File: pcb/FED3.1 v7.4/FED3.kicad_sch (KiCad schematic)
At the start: 29 parts, among them IC2 TB6612FNG, SW1 Sw, U2 MIC5504-3.3, U3 MCP73831T, X5 JST-XH-02

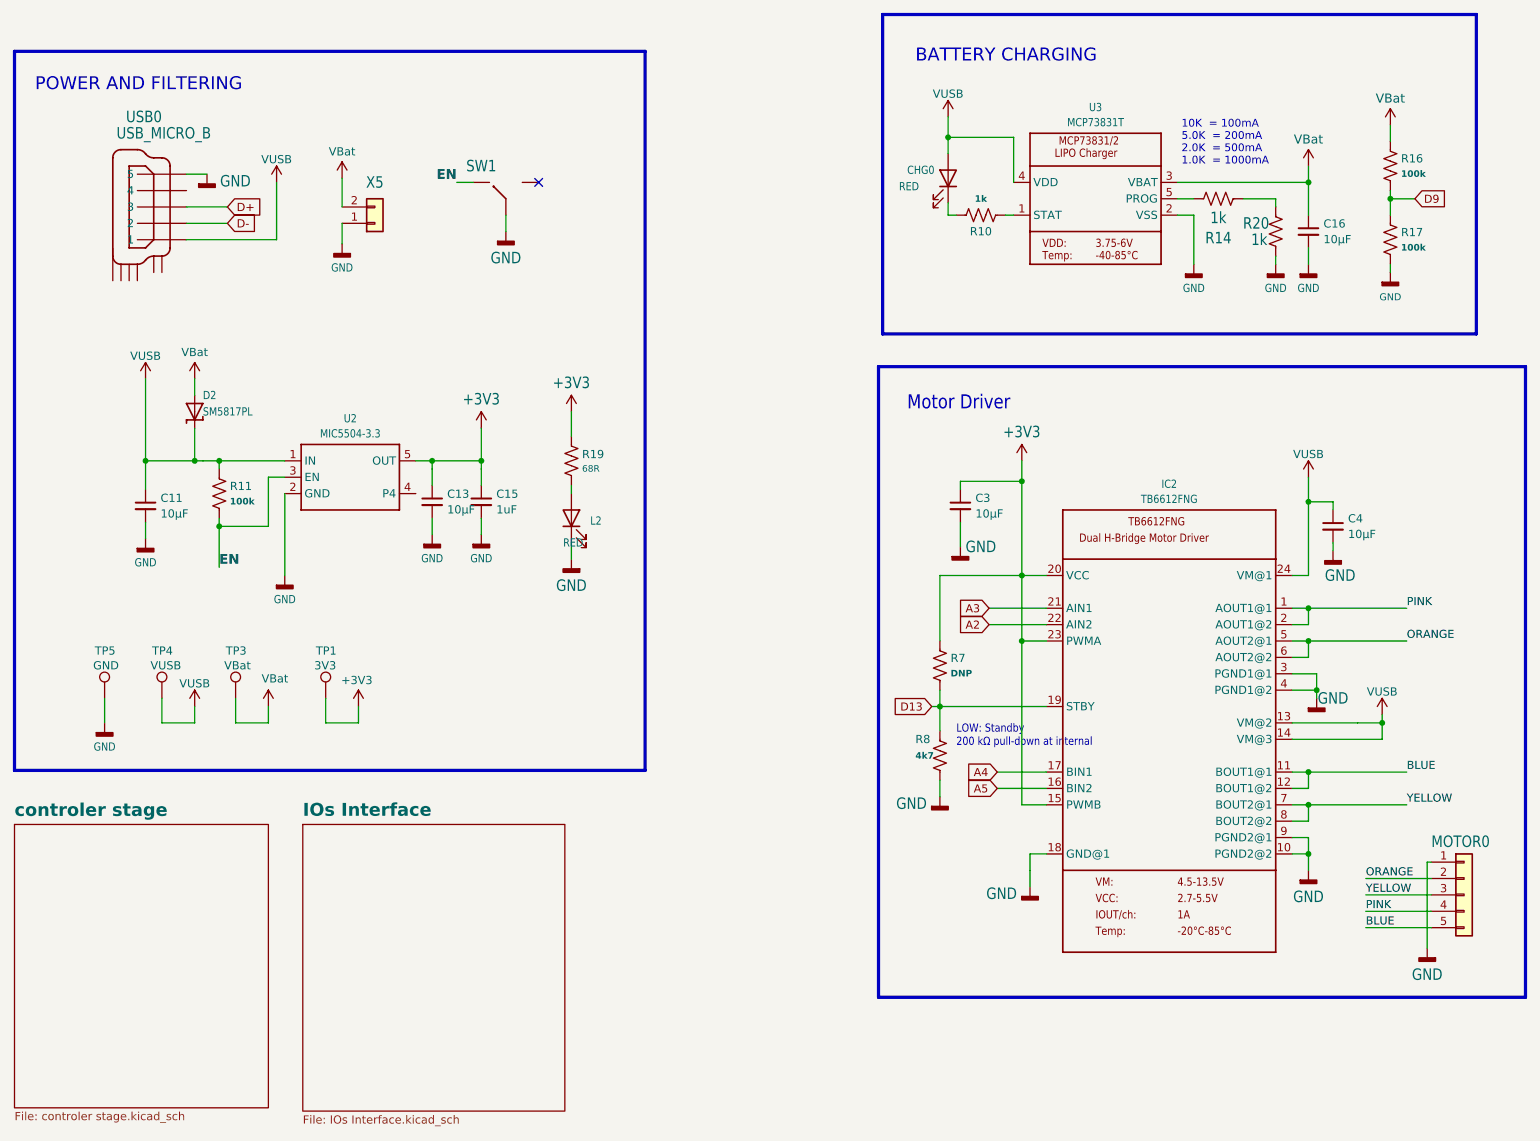
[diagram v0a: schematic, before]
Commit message: review step 2
Realocação de labels e refªs:
- sem qq alteração no circuito
- alteração na PCB apenas a ver com alocação de Designators/SilkScreen parts
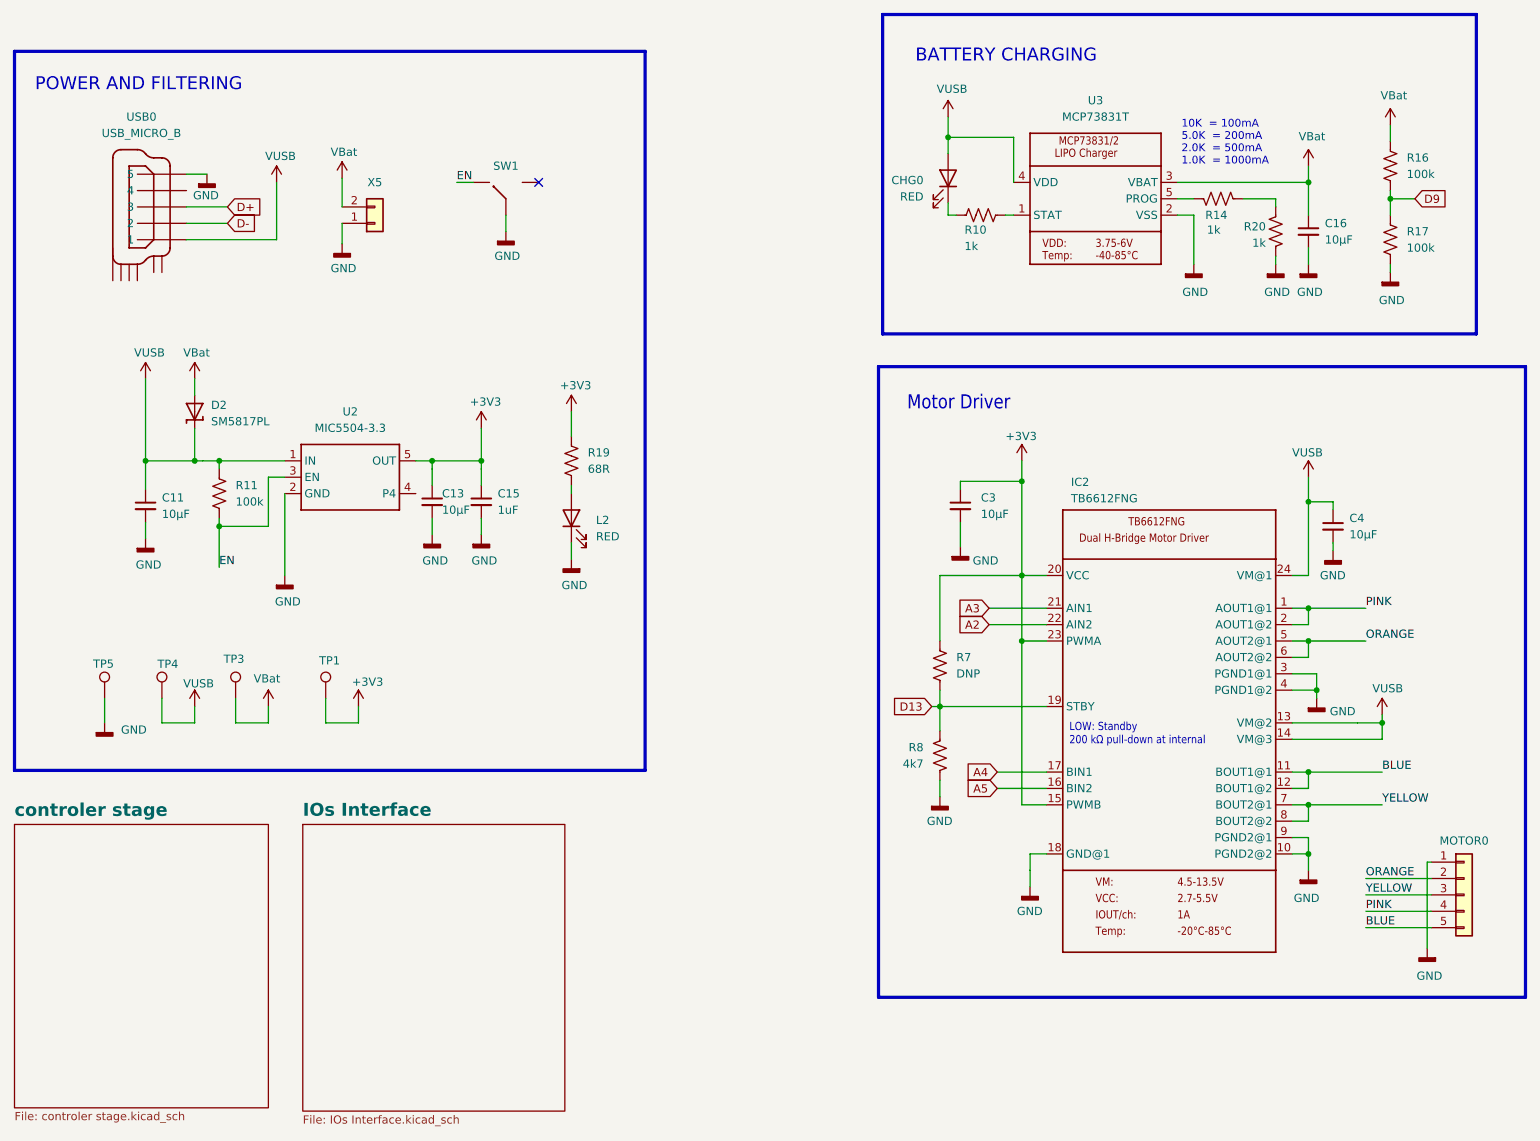
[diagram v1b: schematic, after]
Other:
- moved on the sheet: R20, R8
